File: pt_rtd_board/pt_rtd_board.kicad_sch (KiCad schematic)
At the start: 10 parts, among them J1 Pressure Transducer, J41 Flow Meter Conn 1, U1 HX711_Breakout

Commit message: Modified footprint assignment
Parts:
- U?: footprint (none) -> MAX31865_Breakout:MAX31865_Breakout
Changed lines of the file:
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@@
     (property "Reference" "U?" (id 0) (at 190.881 19.2745 0))
     (property "Value" "MAX31865_Breakout_Board" (id 1) (at 191.262 21.336 0))
-    (property "Footprint" "" (id 2) (at 191.516 38.354 0)
+    (property "Footprint" "MAX31865_Breakout:MAX31865_Breakout" (id 2) (at 191.516 38.354 0)
       (effects (font (size 1.27 1.27)) hide)
     )
@@
     )
     (path "/2dc49687-fe67-4205-a3e3-9eaf94b2e3ab"
-      (reference "U?") (unit 1) (value "MAX31865_Breakout_Board") (footprint "")
-    )
-  )
+      (reference "U?") (unit 1) (value "MAX31865_Breakout_Board") (footprint "MAX31865_Breakout:MAX31865_Breakout")
+    )
+  )

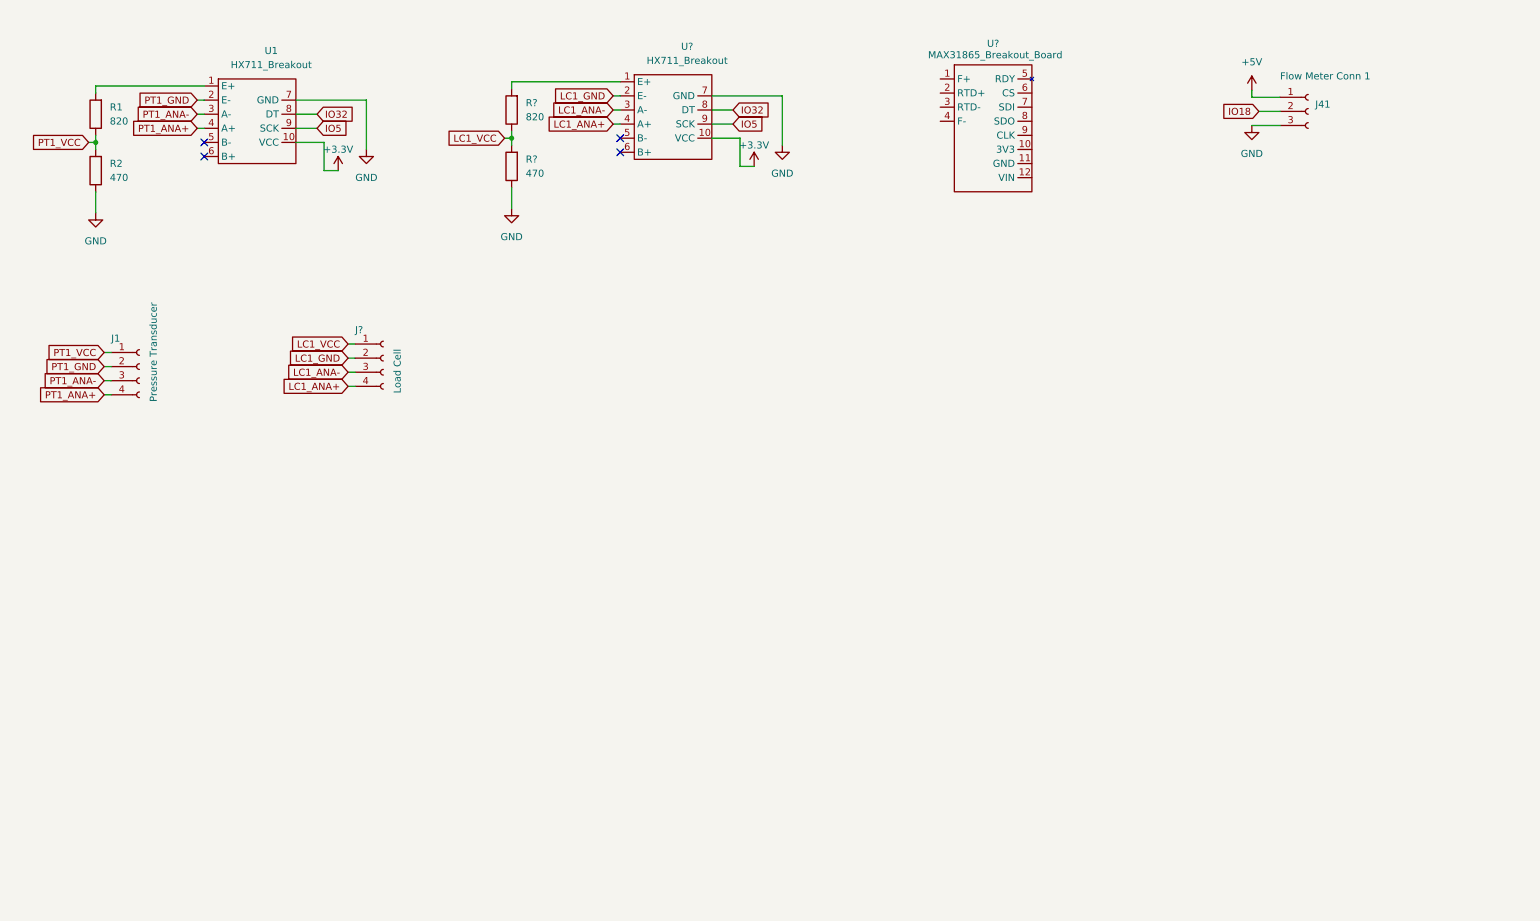
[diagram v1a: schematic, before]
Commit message: updating number of PTs on pt + lc board
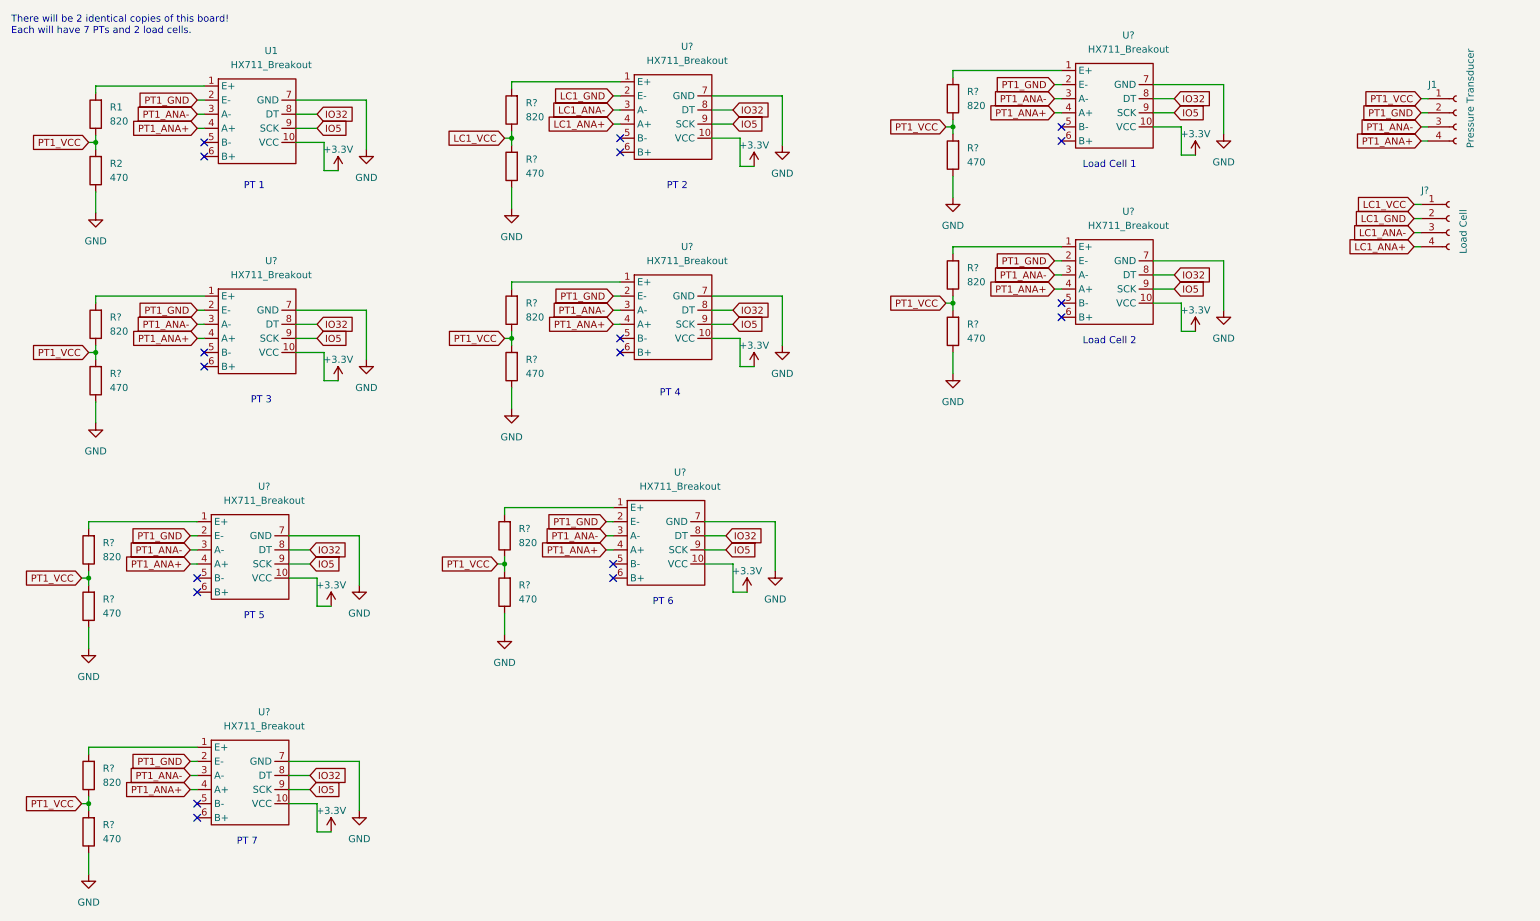
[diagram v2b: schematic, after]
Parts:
- removed J41: Flow Meter Conn 1, Connector_JST:JST_XH_B3B-XH-AM_1x03_P2.50mm_Vertical, symbol Connector:Conn_01x03_Female
- removed U?: MAX31865_Breakout_Board, MAX31865_Breakout:MAX31865_Breakout, symbol le2lib:MAX31865_Breakout_Board
- added R? (x7): 470, Resistor_SMD:R_1206_3216Metric, symbol Device:R
- added R? (x7): 820, Resistor_SMD:R_1206_3216Metric, symbol Device:R
- added U? (x7): HX711_Breakout, Ellie_Project_Footprints:HX711_Breakout_Board, symbol ELLIE_Symbol_Library:HX711_Breakout
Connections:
- net +3V3: now also U?.10 (VCC), U?.10 (VCC), U?.10 (VCC), U?.10 (VCC), U?.10 (VCC), U?.10 (VCC), U?.10 (VCC)
- net GND: now also R?.1, R?.1, R?.1, R?.1, R?.1, R?.1, R?.1, U?.7 (GND), U?.7 (GND), U?.7 (GND), U?.7 (GND), U?.7 (GND), U?.7 (GND), U?.7 (GND)
- net IO32: now also U?.8 (DT), U?.8 (DT), U?.8 (DT), U?.8 (DT), U?.8 (DT), U?.8 (DT), U?.8 (DT)
- net IO5: now also U?.9 (SCK), U?.9 (SCK), U?.9 (SCK), U?.9 (SCK), U?.9 (SCK), U?.9 (SCK), U?.9 (SCK)
- net PT1_ANA+: now also U?.4 (A+), U?.4 (A+), U?.4 (A+), U?.4 (A+), U?.4 (A+), U?.4 (A+), U?.4 (A+)
- net PT1_ANA-: now also U?.3 (A-), U?.3 (A-), U?.3 (A-), U?.3 (A-), U?.3 (A-), U?.3 (A-), U?.3 (A-)
- net PT1_GND: now also U?.2 (E-), U?.2 (E-), U?.2 (E-), U?.2 (E-), U?.2 (E-), U?.2 (E-), U?.2 (E-)
- net PT1_VCC: now also R?.1, R?.1, R?.1, R?.1, R?.1, R?.1, R?.1, R?.2, R?.2, R?.2, R?.2, R?.2, R?.2, R?.2
- new net: R?.2, U?.1 (E+) (x7)
- no-connect marks 4 -> 18
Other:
- note added: "Load Cell 1"
- note added: "Load Cell 2"
- note added: "PT 1"
- note added: "PT 2"
- note added: "PT 3"
- note added: "PT 4"
- note added: "PT 5"
- note added: "PT 6"
- note added: "PT 7"
- note added: "There will be 2 identical copies of this board! Each will have 7 PTs and 2 load cells."
- moved on the sheet: J1, J?

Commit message: board to sensor connections
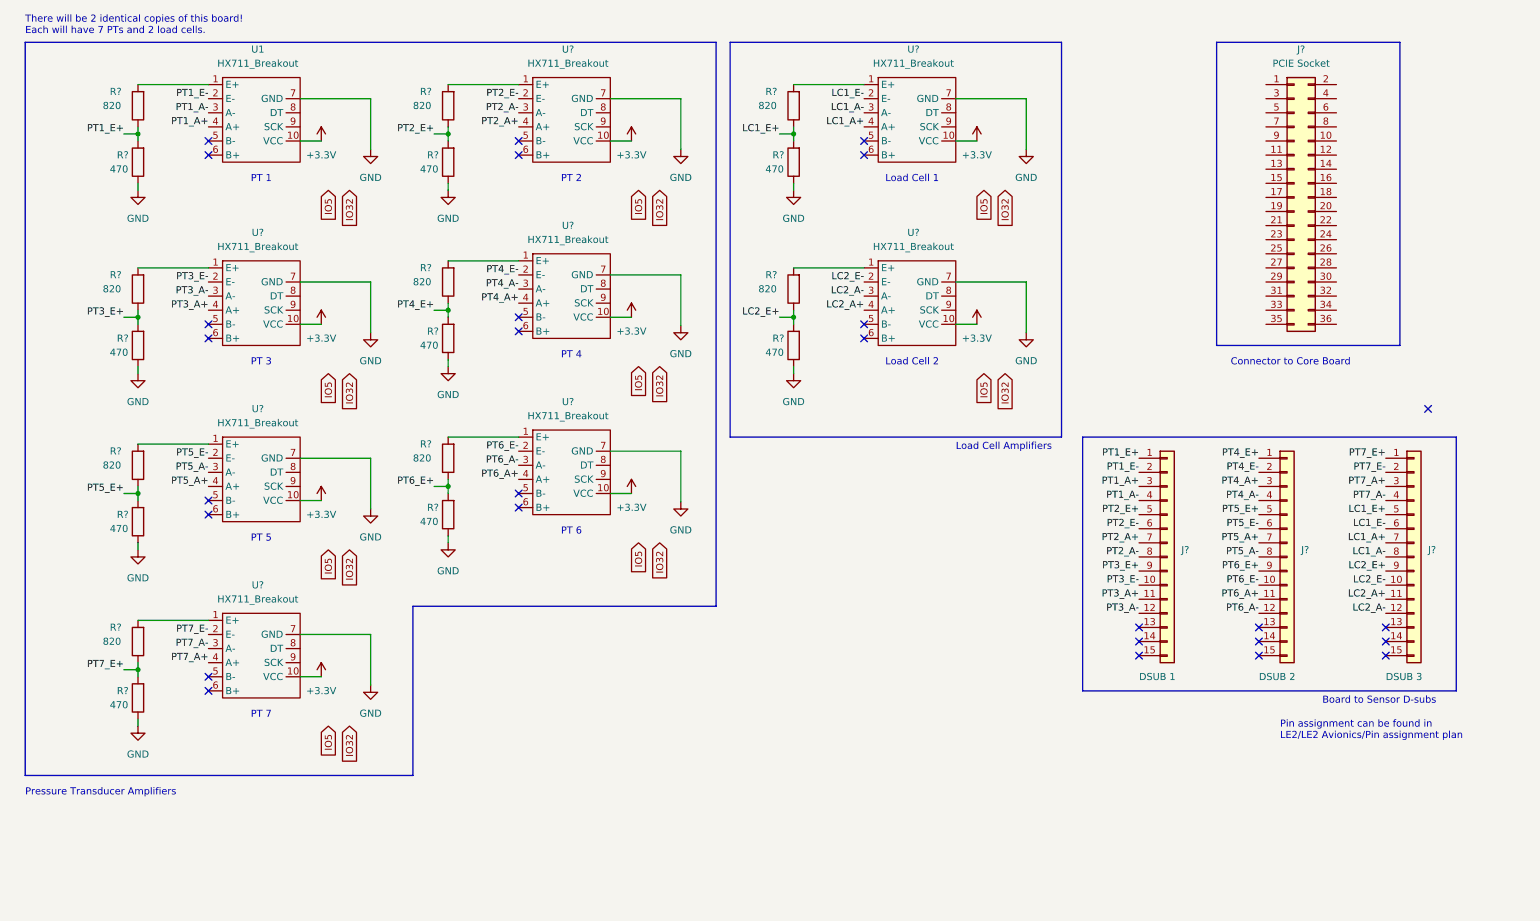
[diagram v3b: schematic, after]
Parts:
- removed J1: Pressure Transducer, Connector_JST:JST_XH_B4B-XH-AM_1x04_P2.50mm_Vertical, symbol Connector:Conn_01x04_Female
- removed J?: Load Cell, Connector_JST:JST_XH_B4B-XH-AM_1x04_P2.50mm_Vertical, symbol Connector:Conn_01x04_Female
- removed R1, R? (x8): 820, Resistor_SMD:R_1206_3216Metric, symbol Device:R
- removed R2, R? (x8): 470, Resistor_SMD:R_1206_3216Metric, symbol Device:R
- removed U? (x8): HX711_Breakout, Ellie_Project_Footprints:HX711_Breakout_Board, symbol ELLIE_Symbol_Library:HX711_Breakout
- added J?: DSUB 2, symbol Connector_Generic:Conn_01x15
- added J?: DSUB 1, symbol Connector_Generic:Conn_01x15
- added J?: DSUB 3, symbol Connector_Generic:Conn_01x15
- added J?: PCIE Socket, symbol Connector_Generic:Conn_02x18_Odd_Even
- added R? (x9): 820, Resistor_SMD:R_1206_3216Metric, symbol Device:R
- added R? (x9): 470, Resistor_SMD:R_1206_3216Metric, symbol Device:R
- added U? (x8): HX711_Breakout, Ellie_Project_Footprints:HX711_Breakout_Board, symbol ELLIE_Symbol_Library:HX711_Breakout
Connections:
- net +3V3: now also U?.10 (VCC), U?.10 (VCC), U?.10 (VCC), U?.10 (VCC), U?.10 (VCC), U?.10 (VCC), U?.10 (VCC), U?.10 (VCC)
- net GND: now also R?.1, R?.1, R?.1, R?.1, R?.1, R?.1, R?.1, R?.1, R?.1, U?.7 (GND), U?.7 (GND), U?.7 (GND), U?.7 (GND), U?.7 (GND), U?.7 (GND), U?.7 (GND), U?.7 (GND)
- net IO32: no longer U1.8 (DT)
- net IO5: no longer U1.9 (SCK)
- net at U1.1 (E+): now also R?.2
- net PT1_ANA+ renamed PT1_A+
- net PT1_A+: now also J?.3 (Pin_3)
- net PT1_ANA- renamed PT1_A-
- net PT1_A-: now also J?.4 (Pin_4)
- net PT1_GND renamed PT1_E-
- net PT1_E-: now also J?.2 (Pin_2)
- new net: R?.2, U?.1 (E+) (x8)
- new net LC1_A+: J?.7 (Pin_7), U?.4 (A+)
- new net LC1_A-: J?.8 (Pin_8), U?.3 (A-)
- new net LC1_E+: J?.5 (Pin_5), R?.1, R?.2
- new net LC1_E-: J?.6 (Pin_6), U?.2 (E-)
- new net LC2_A+: J?.11 (Pin_11), U?.4 (A+)
- new net LC2_A-: J?.12 (Pin_12), U?.3 (A-)
- new net LC2_E+: J?.9 (Pin_9), R?.1, R?.2
- new net LC2_E-: J?.10 (Pin_10), U?.2 (E-)
- new net PT1_E+: J?.1 (Pin_1), R?.1, R?.2
- new net PT2_A+: J?.7 (Pin_7), U?.4 (A+)
- new net PT2_A-: J?.8 (Pin_8), U?.3 (A-)
- new net PT2_E+: J?.5 (Pin_5), R?.1, R?.2
- new net PT2_E-: J?.6 (Pin_6), U?.2 (E-)
- new net PT3_A+: J?.11 (Pin_11), U?.4 (A+)
- new net PT3_A-: J?.12 (Pin_12), U?.3 (A-)
- new net PT3_E+: J?.9 (Pin_9), R?.1, R?.2
- new net PT3_E-: J?.10 (Pin_10), U?.2 (E-)
- new net PT4_A+: J?.3 (Pin_3), U?.4 (A+)
- new net PT4_A-: J?.4 (Pin_4), U?.3 (A-)
- new net PT4_E+: J?.1 (Pin_1), R?.1, R?.2
- new net PT4_E-: J?.2 (Pin_2), U?.2 (E-)
- new net PT5_A+: J?.7 (Pin_7), U?.4 (A+)
- new net PT5_A-: J?.8 (Pin_8), U?.3 (A-)
- new net PT5_E+: J?.5 (Pin_5), R?.1, R?.2
- new net PT5_E-: J?.6 (Pin_6), U?.2 (E-)
- new net PT6_A+: J?.11 (Pin_11), U?.4 (A+)
- new net PT6_A-: J?.12 (Pin_12), U?.3 (A-)
- new net PT6_E+: J?.9 (Pin_9), R?.1, R?.2
- new net PT6_E-: J?.10 (Pin_10), U?.2 (E-)
- new net PT7_A+: J?.3 (Pin_3), U?.4 (A+)
- new net PT7_A-: J?.4 (Pin_4), U?.3 (A-)
- new net PT7_E+: J?.1 (Pin_1), R?.1, R?.2
- new net PT7_E-: J?.2 (Pin_2), U?.2 (E-)
- no-connect marks 18 -> 28
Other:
- note added: "Board to Sensor D-subs"
- note added: "Connector to Core Board"
- note added: "Load Cell Amplifiers"
- note added: "Pin assignment can be found in LE2/LE2 Avionics/Pin assignment plan"
- note added: "Pressure Transducer Amplifiers"
- moved on the sheet: U1

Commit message: adding I2C expander
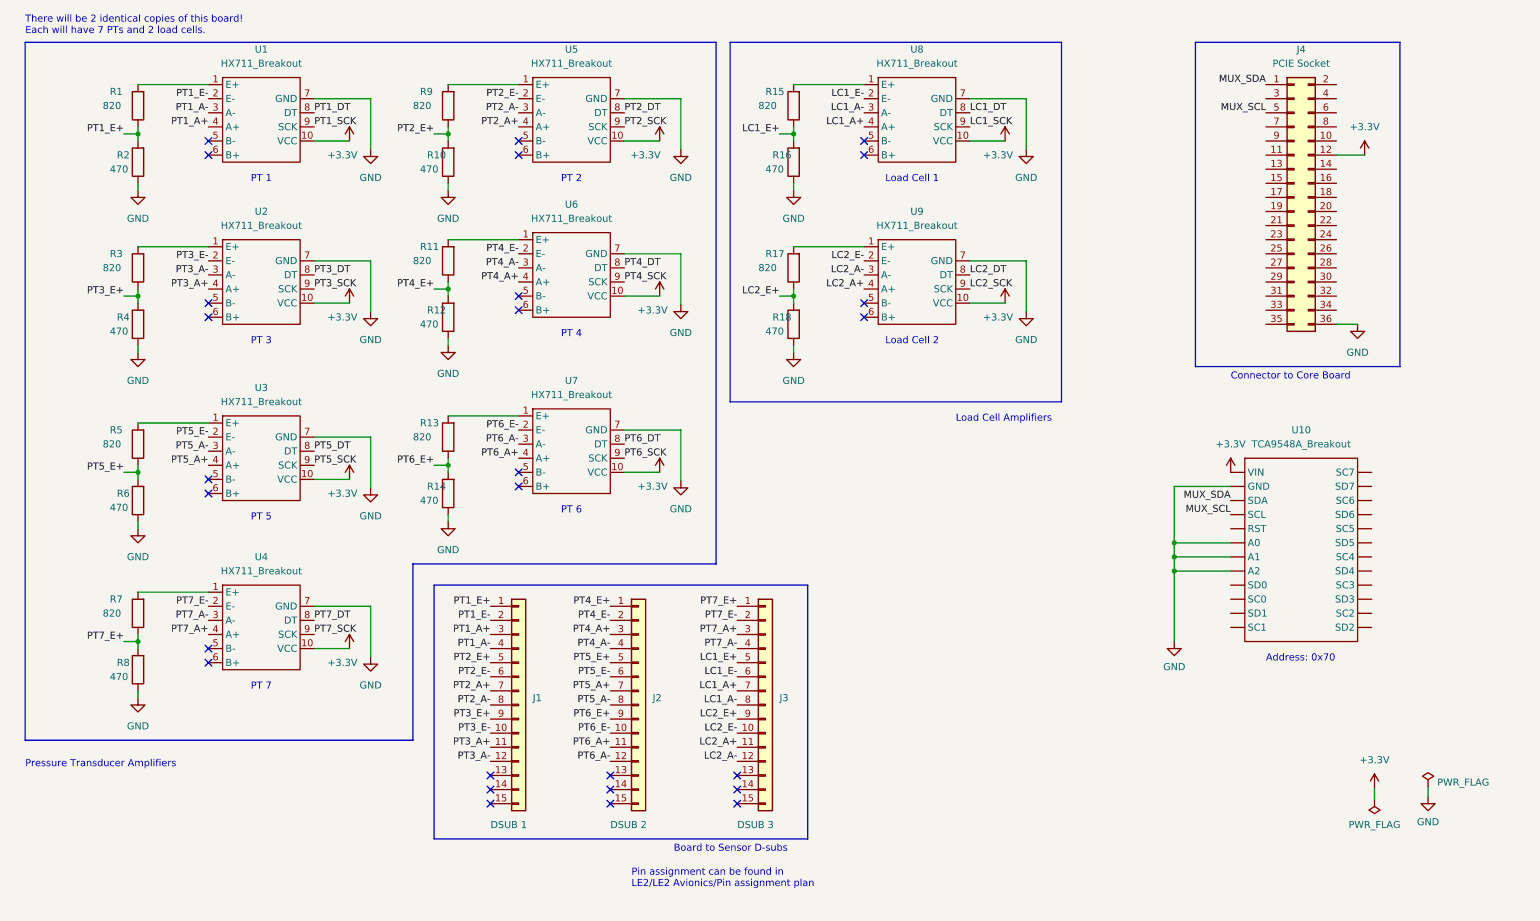
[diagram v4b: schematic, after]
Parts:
- removed U? (x8): HX711_Breakout, Ellie_Project_Footprints:HX711_Breakout_Board, symbol ELLIE_Symbol_Library:HX711_Breakout
- added U10: TCA9548A_Breakout, symbol TCA9548A_Breakout:TCA9548A_Breakout
- added U2, U3, U4, U5, U6, U7, U8, U9: HX711_Breakout, symbol ELLIE_Symbol_Library:HX711_Breakout
- U1: footprint Ellie_Project_Footprints:HX711_Breakout_Board -> (none)
- gave numbers to parts that had none: 22
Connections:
- net +3V3: now also J4.12 (Pin_12), U10. (VIN), U2.10 (VCC), U3.10 (VCC), U4.10 (VCC), U5.10 (VCC), U6.10 (VCC), U7.10 (VCC), U8.10 (VCC), U9.10 (VCC)
- net GND: now also J4.36 (Pin_36), U10. (VIN), U2.7 (GND), U3.7 (GND), U4.7 (GND), U5.7 (GND), U6.7 (GND), U7.7 (GND), U8.7 (GND), U9.7 (GND)
- net LC1_A+: now also U8.4 (A+)
- net LC1_A-: now also U8.3 (A-)
- net LC1_E-: now also U8.2 (E-)
- net LC2_A+: now also U9.4 (A+)
- net LC2_A-: now also U9.3 (A-)
- net LC2_E-: now also U9.2 (E-)
- net PT2_A+: now also U5.4 (A+)
- net PT2_A-: now also U5.3 (A-)
- net PT2_E-: now also U5.2 (E-)
- net PT3_A+: now also U2.4 (A+)
- net PT3_A-: now also U2.3 (A-)
- net PT3_E-: now also U2.2 (E-)
- net PT4_A+: now also U6.4 (A+)
- net PT4_A-: now also U6.3 (A-)
- net PT4_E-: now also U6.2 (E-)
- net PT5_A+: now also U3.4 (A+)
- net PT5_A-: now also U3.3 (A-)
- net PT5_E-: now also U3.2 (E-)
- net PT6_A+: now also U7.4 (A+)
- net PT6_A-: now also U7.3 (A-)
- net PT6_E-: now also U7.2 (E-)
- net PT7_A+: now also U4.4 (A+)
- net PT7_A-: now also U4.3 (A-)
- net PT7_E-: now also U4.2 (E-)
- net at R7.2: now also U4.1 (E+)
- net at R3.2: now also U2.1 (E+)
- net at R5.2: now also U3.1 (E+)
- net at R9.2: now also U5.1 (E+)
- net at R13.2: now also U7.1 (E+)
- net at R15.2: now also U8.1 (E+)
- net PT1_DT: now reaches U1.8 (DT)
- net PT1_SCK: now reaches U1.9 (SCK)
- net at R17.2: now also U9.1 (E+)
- net at R11.2: now also U6.1 (E+)
- net MUX_SDA: now reaches J4.1 (Pin_1)
- net MUX_SDA: now also U10. (VIN)
- net MUX_SCL: now reaches J4.5 (Pin_5)
- net MUX_SCL: now also U10. (VIN)
- new net LC1_DT: U8.8 (DT)
- new net LC1_SCK: U8.9 (SCK)
- new net LC2_DT: U9.8 (DT)
- new net LC2_SCK: U9.9 (SCK)
- new net PT2_DT: U5.8 (DT)
- new net PT2_SCK: U5.9 (SCK)
- new net PT3_DT: U2.8 (DT)
- new net PT3_SCK: U2.9 (SCK)
- new net PT4_DT: U6.8 (DT)
- new net PT4_SCK: U6.9 (SCK)
- new net PT5_DT: U3.8 (DT)
- new net PT5_SCK: U3.9 (SCK)
- new net PT6_DT: U7.8 (DT)
- new net PT6_SCK: U7.9 (SCK)
- new net PT7_DT: U4.8 (DT)
- new net PT7_SCK: U4.9 (SCK)
- no-connect marks 28 -> 27
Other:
- note added: "Address: 0x70"
- moved on the sheet: J1, J2, J3, R11, R12, R13, R14, R17, R18, R3, R4, R5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

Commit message: storing changes
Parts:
- added U?: PCF8575_Breakout, symbol PCF8575_Breakout:PCF8575_Breakout
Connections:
- net +3V3: now also U?.12 (VCC), U?.17 (VDD), U?.9 (VDD)
- net GND: now also U?.10 (GND), U?.11 (GND), U?.16 (GND)
- net MUX_SCL: now also J4.3 (Pin_3); no longer J4.5 (Pin_5)
- new net IO_EXP_SC: U?.14 (SCL)
- new net IO_EXP_SD: U?.13 (SDA)
- no-connect marks 27 -> 28
